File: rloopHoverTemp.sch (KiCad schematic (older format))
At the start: 23 parts, among them P1 CONN_01X01, P2 CONN_01X01, P3 CONN_01X01, P4 CONN_01X01, U1 P82B715TD, U2 MLX90614, U3 Regulator, U4 Regulator, X1 RJ45-SHIELDED, X2 RJ45-SHIELDED

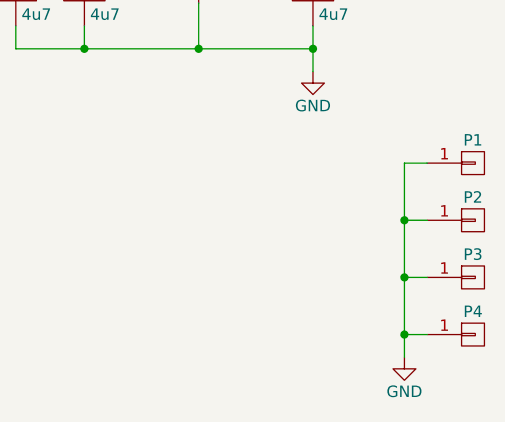
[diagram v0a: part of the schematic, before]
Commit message: removed grounds from screw holes, added a silk label
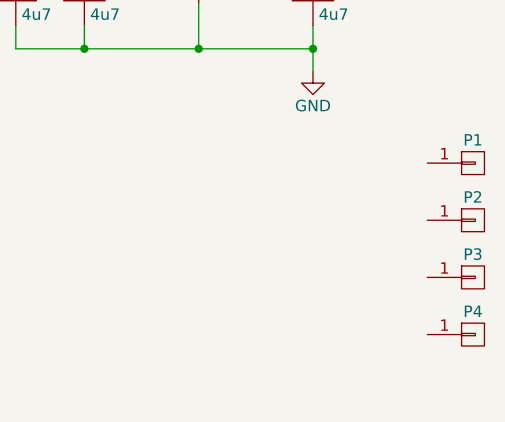
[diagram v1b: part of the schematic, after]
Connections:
- net GND: no longer P1.1 (P1), P2.1 (P1), P3.1 (P1), P4.1 (P1)
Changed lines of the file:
@@
 	2900 3350 3000 3350
 Connection ~ 3000 3350
-$Comp
-L GND #PWR018
-U 1 1 5741470F
-P 10200 5000
-F 0 "#PWR018" H 10200 4750 50  0001 C CNN
-F 1 "GND" H 10200 4850 50  0000 C CNN
-F 2 "" H 10200 5000 50  0000 C CNN
-F 3 "" H 10200 5000 50  0000 C CNN
-	1    10200 5000
-	1    0    0    -1
-$EndComp
-Wire Wire Line
-	10300 4900 10200 4900
-Wire Wire Line
-	10200 4150 10200 5000
-Wire Wire Line
-	10300 4650 10200 4650
-Connection ~ 10200 4900
-Wire Wire Line
-	10300 4400 10200 4400
-Connection ~ 10200 4650
-Wire Wire Line
-	10300 4150 10200 4150
-Connection ~ 10200 4400
 Wire Wire Line
 	2650 3600 2650 3950

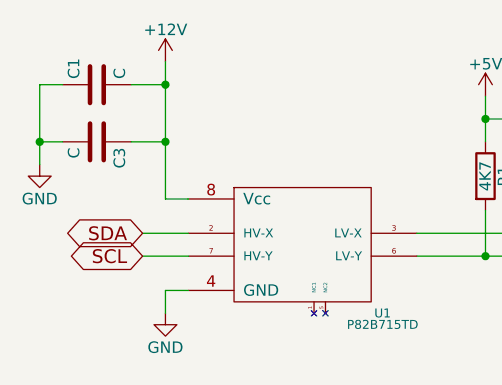
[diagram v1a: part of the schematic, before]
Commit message: missed two capacitor values
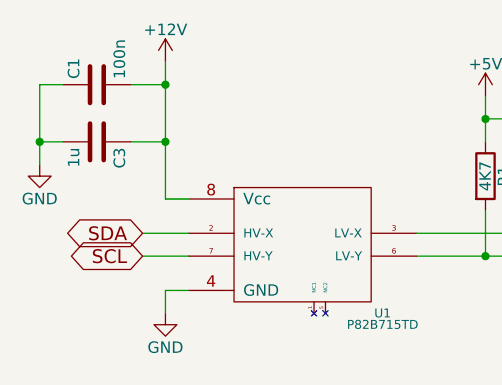
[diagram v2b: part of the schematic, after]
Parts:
- C1: value C -> 100n
- C3: value C -> 1u
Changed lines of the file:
@@
 P 2000 950
 F 0 "C1" H 2025 1050 50  0000 L CNN
-F 1 "C" H 2025 850 50  0000 L CNN
+F 1 "100n" H 2025 850 50  0000 L CNN
 F 2 "Capacitors_SMD:C_0603_HandSoldering" H 2038 800 50  0001 C CNN
 F 3 "" H 2000 950 50  0000 C CNN
@@
 P 2000 1200
 F 0 "C3" H 2025 1300 50  0000 L CNN
-F 1 "C" H 2025 1100 50  0000 L CNN
+F 1 "1u" H 2025 1100 50  0000 L CNN
 F 2 "Capacitors_SMD:C_0603_HandSoldering" H 2038 1050 50  0001 C CNN
 F 3 "" H 2000 1200 50  0000 C CNN
